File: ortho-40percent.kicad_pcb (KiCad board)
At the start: 2 copper layers, 127 parts, among them J1 USB-C_Receptacle-24, SW1 SW_NO_4-Pin, SW10 CherryMX, SW11 CherryMX, SW12 CherryMX, SW13 CherryMX, SW14 CherryMX, SW15 CherryMX, SW16 CherryMX, SW17 CherryMX, SW18 CherryMX, SW19 CherryMX, SW2 CherryMX, SW20 CherryMX, SW21 CherryMX, SW22 CherryMX, SW23 CherryMX, SW24 CherryMX, SW25 CherryMX, SW26 CherryMX, SW27 CherryMX, SW28 CherryMX, SW29 CherryMX, SW3 CherryMX, SW30 CherryMX, SW31 CherryMX, SW32 CherryMX, SW33 CherryMX, SW34 CherryMX, SW35 CherryMX, SW36 CherryMX, SW37 CherryMX, SW38 CherryMX, SW39 CherryMX, SW4 CherryMX, SW40 CherryMX, SW41 CherryMX, SW42 CherryMX, SW43 CherryMX, SW44 CherryMX, SW45 CherryMX, SW46 CherryMX, SW47 CherryMX, SW48 CherryMX, SW49 CherryMX, SW5 CherryMX, SW50 CherryMX, SW51 CherryMX, SW52 CherryMX, SW53 CherryMX, SW6 CherryMX, SW7 CherryMX, SW8 CherryMX, SW9 CherryMX, U1 U_TPD4E05U06DQAR, U2 U_ATmega32u4-AU, Y1 XTAL_4Lead

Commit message: Clarified Keycaps
Added drawing outline of DSA keycap dimension. Added DSA keycap 3d model to 1u mx pcbmount switch. Placed two rows of switches on pcb layout.
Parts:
- SW10, SW11, SW12, SW13, SW14, SW15, SW16, SW17, SW18, SW19, SW20, SW21, SW22, SW23, SW24, SW25, SW26, SW27, SW28, SW29, SW30, SW31, SW32, SW33, SW34, SW35, SW36, SW37, SW38, SW39, SW40, SW41, SW42, SW43, SW44, SW45, SW46, SW47, SW48, SW49, SW6, SW7, SW8, SW9: moved to B.Cu
- moved SW14 485.6 mm to (47.5, 205.9), turned to 270 degrees
- moved SW15 422.1 mm to (66.5, 205.9), turned to 270 degrees
- moved SW17 410.7 mm to (104.5, 205.9), turned to 270 degrees
- moved SW28 408.7 mm to (85.5, 180.5), turned to 270 degrees
- moved SW38 398.8 mm to (47.5, 158.0), turned to 270 degrees
- moved SW10 377.4 mm to (199.5, 224.9), turned to 270 degrees
- moved SW16 369.8 mm to (85.5, 205.9), turned to 270 degrees
- moved SW8 361.0 mm to (161.5, 224.9), turned to 270 degrees
- moved SW27 357.6 mm to (67.0, 181.5), turned to 270 degrees
- moved SW7 353.8 mm to (142.5, 224.9), turned to 270 degrees
- moved SW26 353.2 mm to (48.5, 182.0), turned to 270 degrees
- moved SW29 344.5 mm to (105.5, 181.5), turned to 270 degrees
- moved D17 339.6 mm to (135.5, 210.0), turned to 90 degrees
- moved SW6 324.3 mm to (123.5, 224.9), turned to 270 degrees
- moved SW23 322.7 mm to (218.5, 205.9), turned to 270 degrees
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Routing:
- net /KeyMatrix/COL0: track 0.00 -> 1.41 mm

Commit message: PCB Key Layout
Locked placement of main key matrix on pcb, began placement of matrix diodes.
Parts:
- moved D15 295.9 mm to (97.0, 210.0), turned to 90 degrees
- moved D1 275.6 mm to (59.0, 229.0), turned to 90 degrees
- moved D37 267.0 mm to (59.0, 172.0), turned to 90 degrees
- moved D2 262.4 mm to (78.0, 229.0), turned to 90 degrees
- moved D6 249.4 mm to (154.0, 229.0), turned to 90 degrees
- moved D38 242.4 mm to (78.0, 172.0), turned to 90 degrees
- moved D39 234.3 mm to (97.0, 172.0), turned to 90 degrees
- moved D18 232.3 mm to (154.0, 210.0), turned to 90 degrees
- moved D27 228.3 mm to (97.0, 191.0), turned to 90 degrees
- moved D7 227.1 mm to (173.0, 229.0), turned to 90 degrees
- moved D3 226.5 mm to (97.0, 229.0), turned to 90 degrees
- moved D13 220.5 mm to (189.0, 261.7), turned to 90 degrees
- moved D5 220.5 mm to (189.0, 257.6), turned to 90 degrees
- moved D14 220.5 mm to (194.6, 265.8), turned to 90 degrees
- moved D4 220.5 mm to (194.6, 257.6), turned to 90 degrees
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- renumbered SW33 to SW4

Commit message: Case outline and mounting
Received kprepublic case, used dimensions to set drawing of case and pcb outline. Created M2 screw footprint and added mounting holes to project. Tied screws to power gnd, will possibly change to signal ground later. Changed switches to be kailh hotswaps.
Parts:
- removed D52: D, ortho-40percent:SOD-123
- removed the SW4 at (85.5, 224.9)
- removed the SW4 at (180.5, 186.9)
- removed SW53: CherryMX, CherryMX:SW_Cherry-MX_1U_PCB-Mount
- added H1: H_MountingHole_Screw_withPin, ortho-40percent:H_Screw-M2_Countersunk, F.Cu at (58.9, 135.9)
- added H2: H_MountingHole_Screw_withPin, ortho-40percent:H_Screw-M2_Countersunk, F.Cu at (59.5, 220.5)
- added H3: H_MountingHole_Screw_withPin, ortho-40percent:H_Screw-M2_Countersunk, F.Cu at (64.8, 135.9)
- added H4: H_MountingHole_Screw_withPin, ortho-40percent:H_Screw-M2_Countersunk, F.Cu at (64.8, 141.8)
- added H5: H_MountingHole_Screw_withPin, ortho-40percent:H_Screw-M2_Countersunk, F.Cu at (71.5, 136.0)
- added SW33: CherryMX, CherryMX:SW_Cherry-MX_1U_PCB-Mount_Kailh-Hot-Swap, B.Cu at (180.5, 186.9)
- added SW4: CherryMX, CherryMX:SW_Cherry-MX_1U_PCB-Mount_Kailh-Hot-Swap, B.Cu at (85.5, 224.9)
- SW10, SW11, SW12, SW13, SW14, SW15, SW16, SW17, SW18, SW19, SW2, SW20, SW21, SW22, SW23, SW24, SW25, SW26, SW27, SW28, SW29, SW3, SW30, SW31, SW32, SW34, SW35, SW36, SW37, SW38, SW39, SW40, SW41, SW42, SW43, SW44, SW45, SW46, SW47, SW48, SW49, SW5, SW50, SW51, SW52, SW6, SW7, SW8, SW9: footprint CherryMX:SW_Cherry-MX_1U_PCB-Mount -> CherryMX:SW_Cherry-MX_1U_PCB-Mount_Kailh-Hot-Swap
- moved SW51 197.3 mm to (202.0, 113.5)
- moved SW50 191.0 mm to (182.0, 114.0)
- moved SW52 176.9 mm to (182.5, 135.0)
- moved D50 166.1 mm to (230.0, 125.5)
- moved D51 164.2 mm to (223.0, 126.5)
- moved D49 142.2 mm to (222.5, 115.0)
- moved D13 138.1 mm to (58.0, 218.0)
- moved D14 126.9 mm to (77.0, 218.0)
- moved D25 125.2 mm to (58.0, 199.0)
- moved D26 106.9 mm to (77.0, 199.0)
- moved D41 101.7 mm to (134.0, 180.0)
- moved D23 101.3 mm to (248.0, 218.0)
- moved D40 101.0 mm to (115.0, 180.0)
- moved D42 83.9 mm to (153.0, 180.0)
- moved D33 83.9 mm to (210.0, 199.0)
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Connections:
- U2 pad 14: Net-(U2-Pad14) -> VCC
- U2 pad 2: Net-(U2-Pad14) -> VCC
- U2 pad 24: Net-(U2-Pad14) -> VCC
- U2 pad 34: Net-(U2-Pad14) -> VCC
- U2 pad 44: Net-(U2-Pad14) -> VCC
- U2 pad 7: Net-(U2-Pad14) -> VCC
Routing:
- net /KeyMatrix/COL0: track 1.41 -> 0.00 mm
- net (no net): track 0.00 -> 1.41 mm
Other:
- board outline added: 229 x 77 mm

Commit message: ESD overhaul and mechanical finish
Finished mounting hole placement with respect to case dimensions. Rotated all switches 180 to allow for placement of USB-C connector. Redid ground connections to have connector shield grounded to case and signal ground grounded to case, but not connected on PCB. Added tab on PCB edge to allow USB-C connector to extend further out of case. Replaced 9V TVS with 6V TVS.
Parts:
- H1, H2, H3, H4, H5: moved to B.Cu
- TVS1: value TVS_Bidirectional -> TVS_Unidirectional
- moved L1 230.1 mm to (321.0, 188.5)
- moved R2 201.0 mm to (311.0, 194.5), turned to 90 degrees
- moved H5 197.0 mm to (249.5, 220.5)
- moved R1 197.0 mm to (313.5, 194.5), turned to 90 degrees
- moved F1 194.3 mm to (304.5, 199.0), turned to 90 degrees
- moved H4 189.2 mm to (249.5, 182.5)
- moved TVS1 173.8 mm to (297.5, 196.5), turned to 270 degrees
- moved SW50 145.6 mm to (37.0, 101.0)
- moved SW52 145.6 mm to (37.5, 122.0)
- moved SW51 140.2 mm to (62.0, 105.5)
- moved U1 129.3 mm to (231.0, 171.5), turned to 90 degrees
- moved H3 111.1 mm to (154.5, 201.5)
- moved D49 86.0 mm to (294.5, 162.0)
- moved D50 86.0 mm to (302.0, 172.5)
- moved D51 86.0 mm to (295.0, 173.5)
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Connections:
- H1 pad 1: GNDPWR -> GND
- H2 pad 1: GNDPWR -> GND
- H3 pad 1: GNDPWR -> GND
- H5 pad 1: GNDPWR -> GND
- J1 pad A1: GNDPWR -> GND
- J1 pad B1: GNDPWR -> GND
- J1 pad S: Net-(J1-PadS) -> GNDPWR
- R1 pad 1: GNDPWR -> GND
- R2 pad 1: GNDPWR -> GND
- TVS1 pad A: GNDPWR -> GND
- U1 pad 3: GNDPWR -> GND
- U1 pad 8: GNDPWR -> GND
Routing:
- net (no net): track 1.41 -> 0.00 mm
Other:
- board size 229 x 77 mm -> 229 x 81 mm

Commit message: 2u footprint and plate comments
Finished 2u footprint in all styles. Added cutouts by using Cmts.User layer.
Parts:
- SW50, SW51, SW52: footprint CherryMX:SW_Cherry-MX_1U_PCB-Mount_Kailh-Hot-Swap -> CherryMX:SW_Cherry-MX_2U_PCB-Mount_Kailh-Hot-Swap; moved to B.Cu
- moved SW50 216.5 mm to (173.5, 269.0), turned to 270 degrees
- moved SW52 176.7 mm to (135.5, 269.0), turned to 270 degrees
- moved SW51 169.6 mm to (154.0, 248.0), turned to 270 degrees
- moved F1 90.0 mm to (220.0, 168.0)
- moved L1 84.4 mm to (242.5, 157.5), turned to 90 degrees
- moved TVS1 79.8 mm to (223.0, 168.0)
- moved R1 71.3 mm to (253.5, 156.0)
- moved R2 71.3 mm to (251.0, 156.0)
- moved C6 42.1 mm to (105.0, 145.5), turned to 270 degrees
- moved C9 35.1 mm to (117.0, 145.5), turned to 270 degrees
- moved C2 32.7 mm to (109.0, 141.5), turned to 270 degrees
- moved C8 32.7 mm to (113.0, 145.5), turned to 270 degrees
- moved C7 31.2 mm to (109.0, 145.5), turned to 270 degrees
- moved C1 30.5 mm to (105.0, 141.5), turned to 270 degrees
- moved C5 23.2 mm to (117.0, 141.5), turned to 270 degrees
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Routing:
- net GNDPWR: track 0.00 -> 25.6 mm

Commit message: Fixed case, pcb, screw locations
Set origin to hole on bottom-left switch, based all pcb and case dimensions on that hole. Relocated screws to new locations, now they are symmetrical with key positions.
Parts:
- removed D51: D, ortho-40percent:SOD-123
- removed SW52: CherryMX, CherryMX:SW_Cherry-MX_2U_PCB-Mount_Kailh-Hot-Swap
- moved SW50 60.0 mm to (132.9, 224.8)
- moved SW51 28.7 mm to (170.9, 224.8)
- moved L1 21.8 mm to (224.0, 146.0)
- moved R2 20.4 mm to (233.0, 146.5)
- moved R1 17.0 mm to (238.5, 148.0)
- moved SW15 1.00 mm to (71.5, 216.0)
- moved SW27 1.00 mm to (71.5, 197.0)
- moved SW3 1.00 mm to (71.5, 235.0)
- moved SW39 1.00 mm to (71.5, 178.0)
- moved H1 0.09 mm to (59.5, 182.4)
- moved H2 0.09 mm to (59.5, 220.4)
- moved H3 0.09 mm to (154.5, 201.4)
- moved H4 0.09 mm to (249.5, 182.4)
- moved H5 0.09 mm to (249.5, 220.4)
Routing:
- net GNDPWR: track 25.6 -> 0.00 mm
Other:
- outline, holes or cut-outs redrawn

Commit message: Micro change and origin reset
Returned origin to center hole of bottom-left switch instead of pin 1 hole.
Added 3mm ground trace margin and mtg hole margin.
Created 44-VQFN footprint and schematic symbol, and updated micro to new part.
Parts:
- U2: value U_ATmega32u4-AU -> U_ATmega32u4-MU; footprint ortho-40percent:TQFP-44 -> ortho-40percent:VQFN-44-1EP_7x7mm_P0.5mm_ThermalVias
- moved D50 98.4 mm to (207.0, 146.9)
- moved D49 92.8 mm to (203.0, 146.9)
- moved U2 70.0 mm to (150.0, 134.9)
- moved Y1 50.2 mm to (150.0, 142.4), turned to 180 degrees
- moved C7 49.0 mm to (156.5, 133.4)
- moved C1 48.5 mm to (153.5, 142.4), turned to 90 degrees
- moved C8 44.1 mm to (156.5, 137.9)
- moved C6 39.2 mm to (143.5, 137.9), turned to 90 degrees
- moved C2 37.5 mm to (146.5, 142.4)
- moved L1 36.5 mm to (260.0, 152.4)
- moved C9 34.5 mm to (147.0, 128.4), turned to 90 degrees
- moved C4 31.5 mm to (143.5, 133.4), turned to 90 degrees
- moved C5 29.5 mm to (143.5, 128.4), turned to 90 degrees
- moved D40 18.9 mm to (101.0, 167.9), turned to 270 degrees
- moved D15 18.5 mm to (82.0, 205.9), turned to 270 degrees
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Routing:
- net GNDPWR: track 0.00 -> 25.4 mm

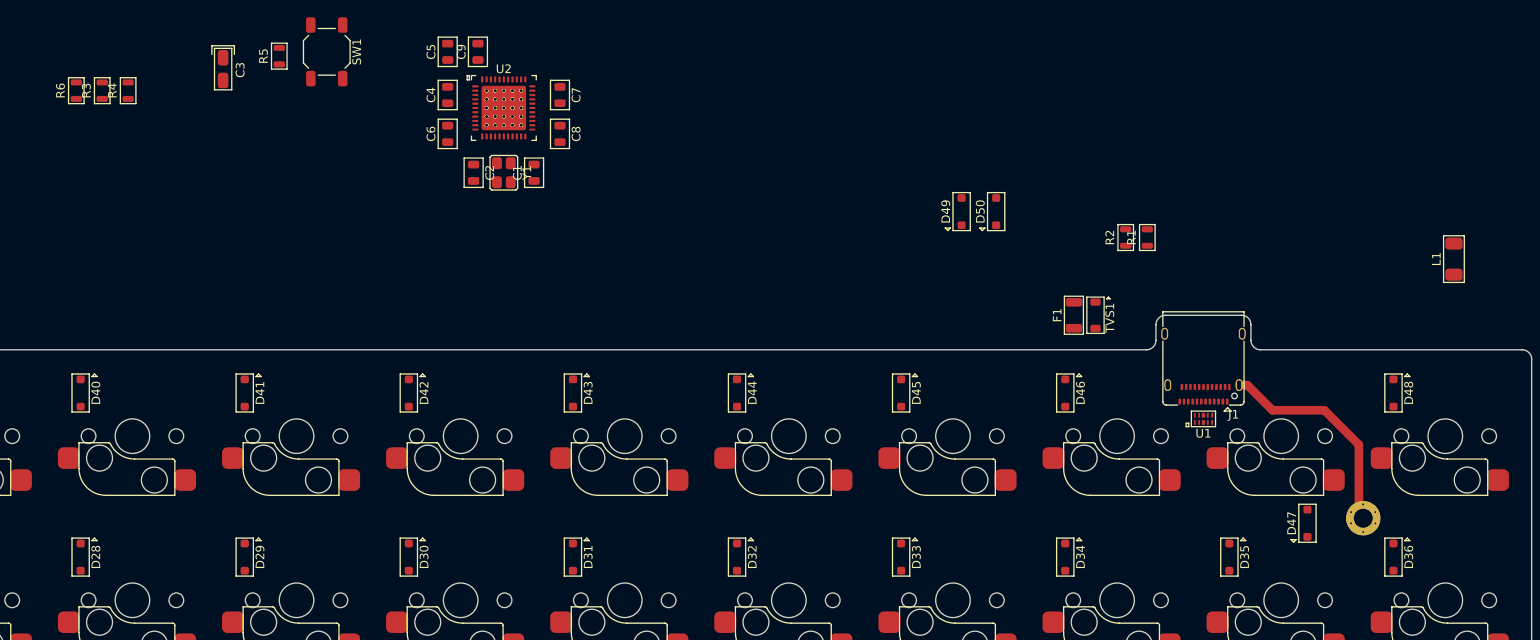
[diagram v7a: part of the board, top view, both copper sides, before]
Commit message: USB connector update
Added connector keepout zone and PCB edge text for usb-c connector footprint. Attempted routing and movement of D+/D- lines.
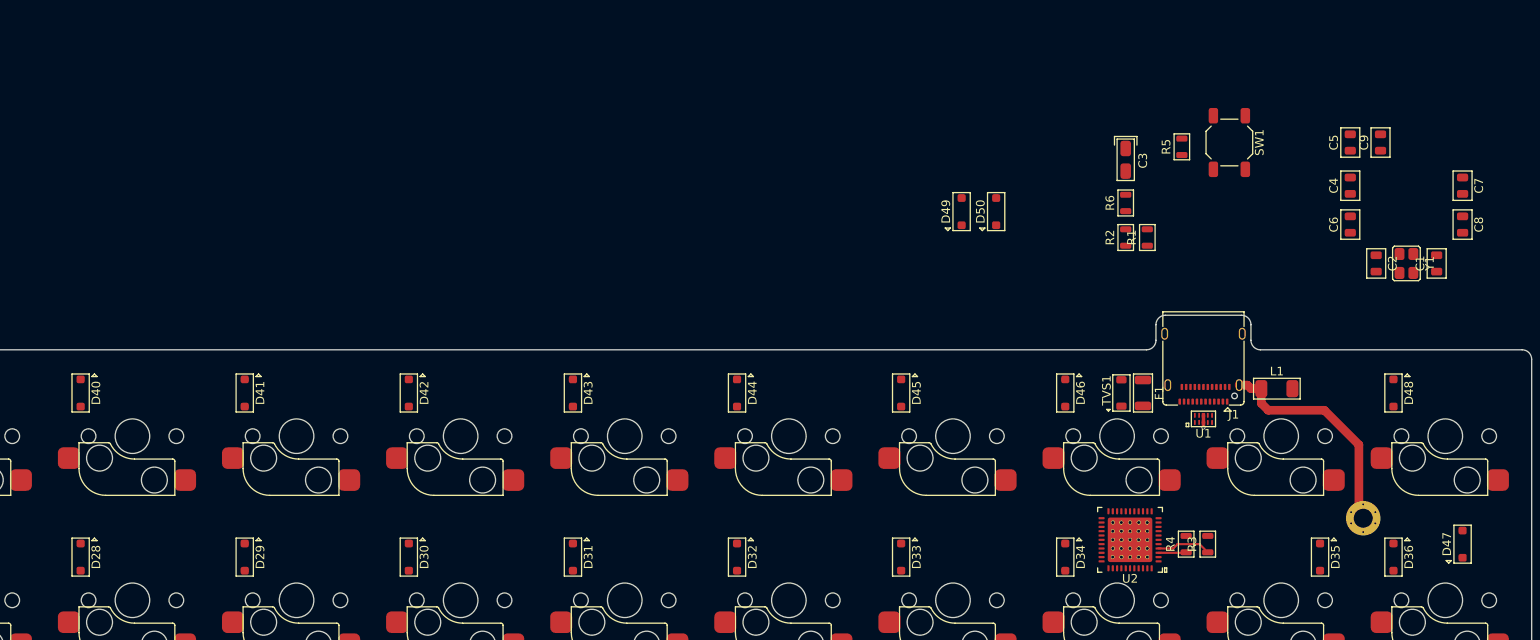
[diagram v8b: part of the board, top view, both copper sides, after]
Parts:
- moved R3 138.3 mm to (231.5, 185.4)
- moved R4 133.3 mm to (229.0, 185.4)
- moved R6 122.2 mm to (222.0, 145.9)
- moved C3 105.0 mm to (222.0, 140.9)
- moved R5 105.0 mm to (228.5, 139.4)
- moved C2 105.0 mm to (251.0, 152.9)
- moved C4 105.0 mm to (248.0, 143.9)
- moved C5 105.0 mm to (248.0, 138.9)
- moved C6 105.0 mm to (248.0, 148.4)
- moved C9 105.0 mm to (251.5, 138.9)
- moved SW1 105.0 mm to (234.0, 138.9)
- moved Y1 105.0 mm to (254.5, 152.9)
- moved C1 105.0 mm to (258.0, 152.9)
- moved C7 105.0 mm to (261.0, 143.9)
- moved C8 105.0 mm to (261.0, 148.4)
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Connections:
- net Net-(R3-Pad1) renamed /D+
- net Net-(R4-Pad1) renamed /D-
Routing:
- net /D+: track 0.00 -> 6.30 mm
- net /D-: track 0.00 -> 3.22 mm
- net GND: track 0.00 -> 1.42 mm, vias 0 -> 1
- net GNDPWR: track 25.4 -> 26.4 mm
